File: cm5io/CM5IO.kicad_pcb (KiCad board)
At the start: 4 copper layers, 160 x 90 mm, 56 parts, among them J11 USB_C_Receptacle_USB2.0, J12 USB3_A, J14 JST_SHBM04B-SRSS-TB, J22 690-019-298-412, J3 Conn_01x03, J4 Bus_M.2_Socket_M, J7 Micro_SD_Card_Det, SW1 Right angle Tact button, U12 RT9742SNGV, U18 RT9742GGJ5, U5 74LVC1G07SE-7, U6 AP22653W6, U7 ASEK-32.768KHZ-L-R-T, U8 AP3441SHE-7B

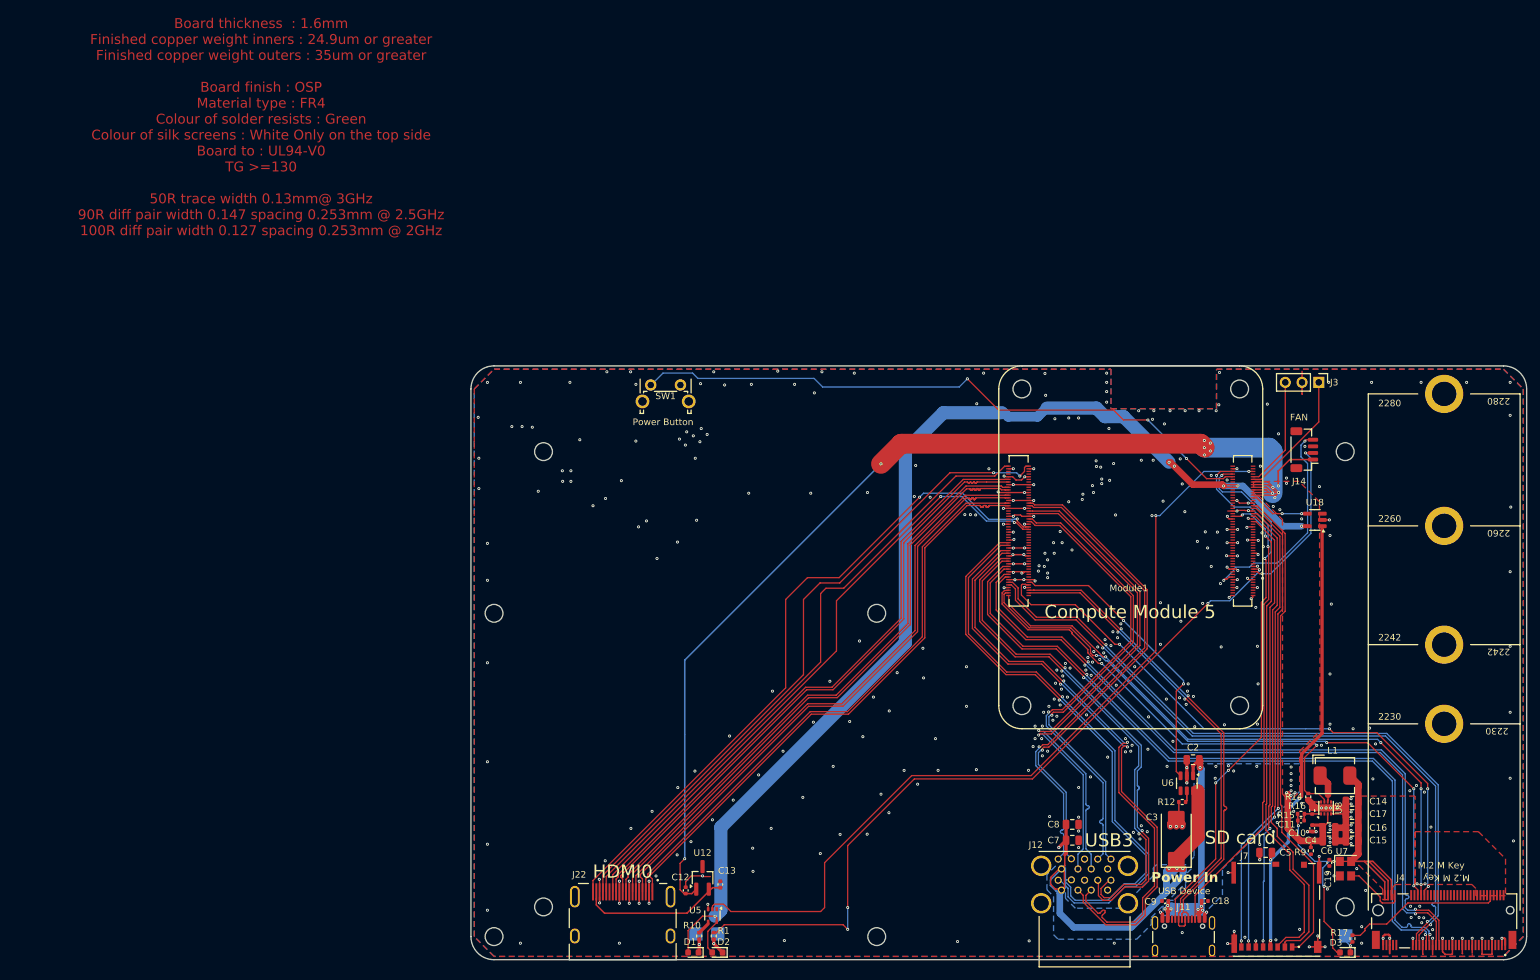
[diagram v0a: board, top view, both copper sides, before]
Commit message: [cm5io] remove USB-C and NVMe connectors, clean up routing
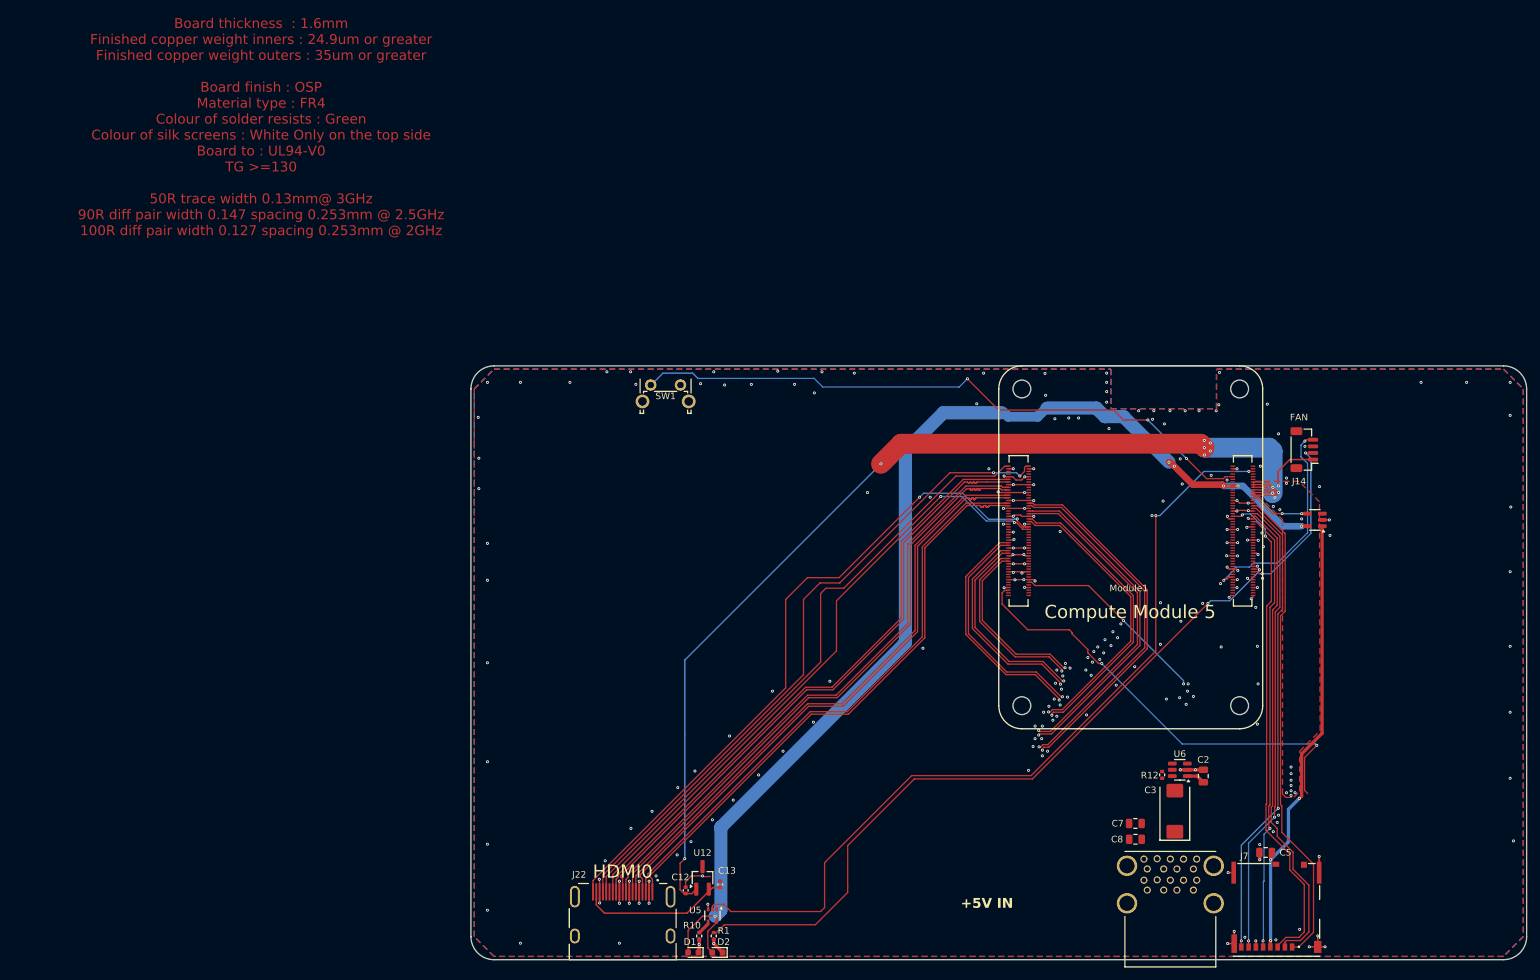
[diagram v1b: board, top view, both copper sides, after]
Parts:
- removed C10, C18, C19, C9: 100n, Capacitor_SMD:C_0402_1005Metric
- removed C11: 4.7nF, Capacitor_SMD:C_0402_1005Metric
- removed C14, C15, C16, C17, C4, C6: 10u, Capacitor_SMD:C_0805_2012Metric
- removed D3: LED Green, LED_SMD:LED_0603_1608Metric
- removed H1, H2, H3, H4, H5, H6, H7, H8: MountingHole, CM5IO:MountingHole_2.7mm_M2.5_DIN965
- removed J11: USB_C_Receptacle_USB2.0, Connector_USB:USB_C_Receptacle_GCT_USB4105-xx-A_16P_TopMnt_Horizontal
- removed J3: Conn_01x03, Connector_PinHeader_2.54mm:PinHeader_1x03_P2.54mm_Vertical
- removed J4: Bus_M.2_Socket_M, CM5IO:M.2 M Key socket
- removed L1: 2.2uH, CM5IO:L_Bourns_SRP5030CC
- removed R14: 100K 1%, Resistor_SMD:R_0402_1005Metric
- removed R15: 10K 1%, Resistor_SMD:R_0402_1005Metric
- removed R16, R9: 2.2K 1%, Resistor_SMD:R_0402_1005Metric
- removed R17: 1k, Resistor_SMD:R_0402_1005Metric
- removed TP1, TP3, TP5: TestPoint, TestPoint:TestPoint_Pad_2.0x2.0mm
- removed U7: ASEK-32.768KHZ-L-R-T, Crystal:Crystal_SMD_3225-4Pin_3.2x2.5mm
- removed U8: AP3441SHE-7B, Package_DFN_QFN:DFN-8-1EP_2x2mm_P0.5mm_EP1.05x1.75mm
- SW1: value Right angle Tact button -> Power button
- moved J12 13.0 mm to (185.0, 151.4)
- moved C7 9.88 mm to (179.7, 139.3), turned to 180 degrees
- moved C8 9.84 mm to (179.7, 141.8), turned to 180 degrees
- moved R12 5.11 mm to (183.8, 132.0), turned to -90 degrees
- moved C3 4.11 mm to (185.7, 137.5)
- moved C2 2.91 mm to (190.0, 132.2), turned to 90 degrees
- moved U6 2.30 mm to (186.4, 131.2), turned to 180 degrees
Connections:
- Module1 pad 103: /USB2_N -> /CM5_HighSpeed/USB2_N
- Module1 pad 105: /USB2_P -> /CM5_HighSpeed/USB2_P
- Module1 pad 89: /CM5_GPIO ( Ethernet, GPIO, SDCARD)/WL_nDis -> unconnected-(Module1A-WiFi_nDisable-Pad89)
- Module1 pad 91: /CM5_GPIO ( Ethernet, GPIO, SDCARD)/BT_nDis -> unconnected-(Module1A-BT_nDisable-Pad91)
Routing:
- net GND: track 708.4 -> 112.4 mm, vias 429 -> 242
- net /CM5_HighSpeed/PCIE_TX_N: track 109.5 -> 0.00 mm, vias 2 -> 0
- net /CM5_HighSpeed/PCIE_TX_P: track 109.5 -> 0.00 mm, vias 2 -> 0
- net /CM5_HighSpeed/PCIE_RX_N: track 107.9 -> 0.00 mm, vias 2 -> 0
- net /CM5_HighSpeed/PCIE_RX_P: track 107.8 -> 0.00 mm, vias 2 -> 0
- net /CM5_HighSpeed/PCIE_CLK_N: track 103.8 -> 0.00 mm, vias 2 -> 0
- net /CM5_HighSpeed/PCIE_CLK_P: track 103.8 -> 0.00 mm, vias 2 -> 0
- net /CM5_HighSpeed/PCIE_nRST: track 93.4 -> 0.00 mm, vias 4 -> 0
- net /CM5_HighSpeed/PCIE_nWAKE: track 92.7 -> 0.00 mm, vias 4 -> 0
- net /CM5_HighSpeed/PCIE_nCLKREQ: track 92.1 -> 0.00 mm, vias 4 -> 0
- net /CM5_HighSpeed/VBUS: track 80.6 -> 0.00 mm, vias 4 -> 0
- net /CC1: track 80.3 -> 0.00 mm, vias 4 -> 0
- net /CC2: track 79.2 -> 0.00 mm, vias 2 -> 0
- net /USB2_N: track 71.9 -> 0.00 mm, vias 2 -> 0
- net /USB2_P: track 71.7 -> 0.00 mm, vias 2 -> 0
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- removed copper zone on B.Cu, net /+5v
- removed copper zone on B.Cu, net /CM5_HighSpeed/VBUS
- removed copper zone on F.Cu, net /PCIe-M2/M2_3v3
- removed copper zone on In2.Cu, net GND
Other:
- board text added: "+5V IN"
- board text removed: "M.2 M Key"
- board text removed: "Power Button"
- board text removed: "Power In"
- board text removed: "SD card"
- board text removed: "USB Device"
- board text removed: "USB3"
